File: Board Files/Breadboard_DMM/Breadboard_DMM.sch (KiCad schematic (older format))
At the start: 11 parts

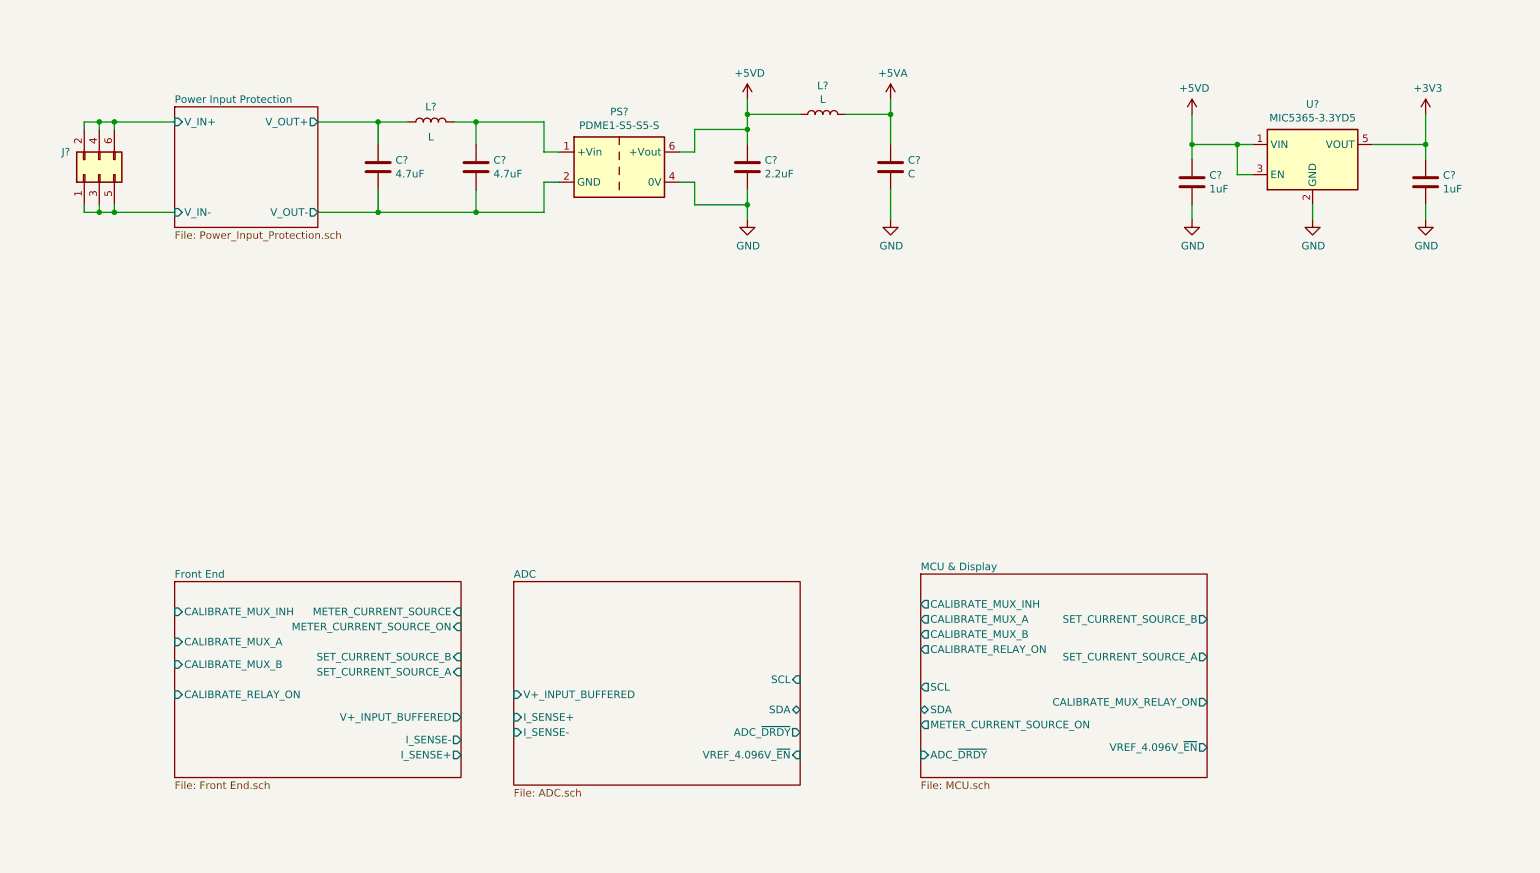
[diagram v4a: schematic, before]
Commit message: Finished main cleanup, started adding digikey part numbers
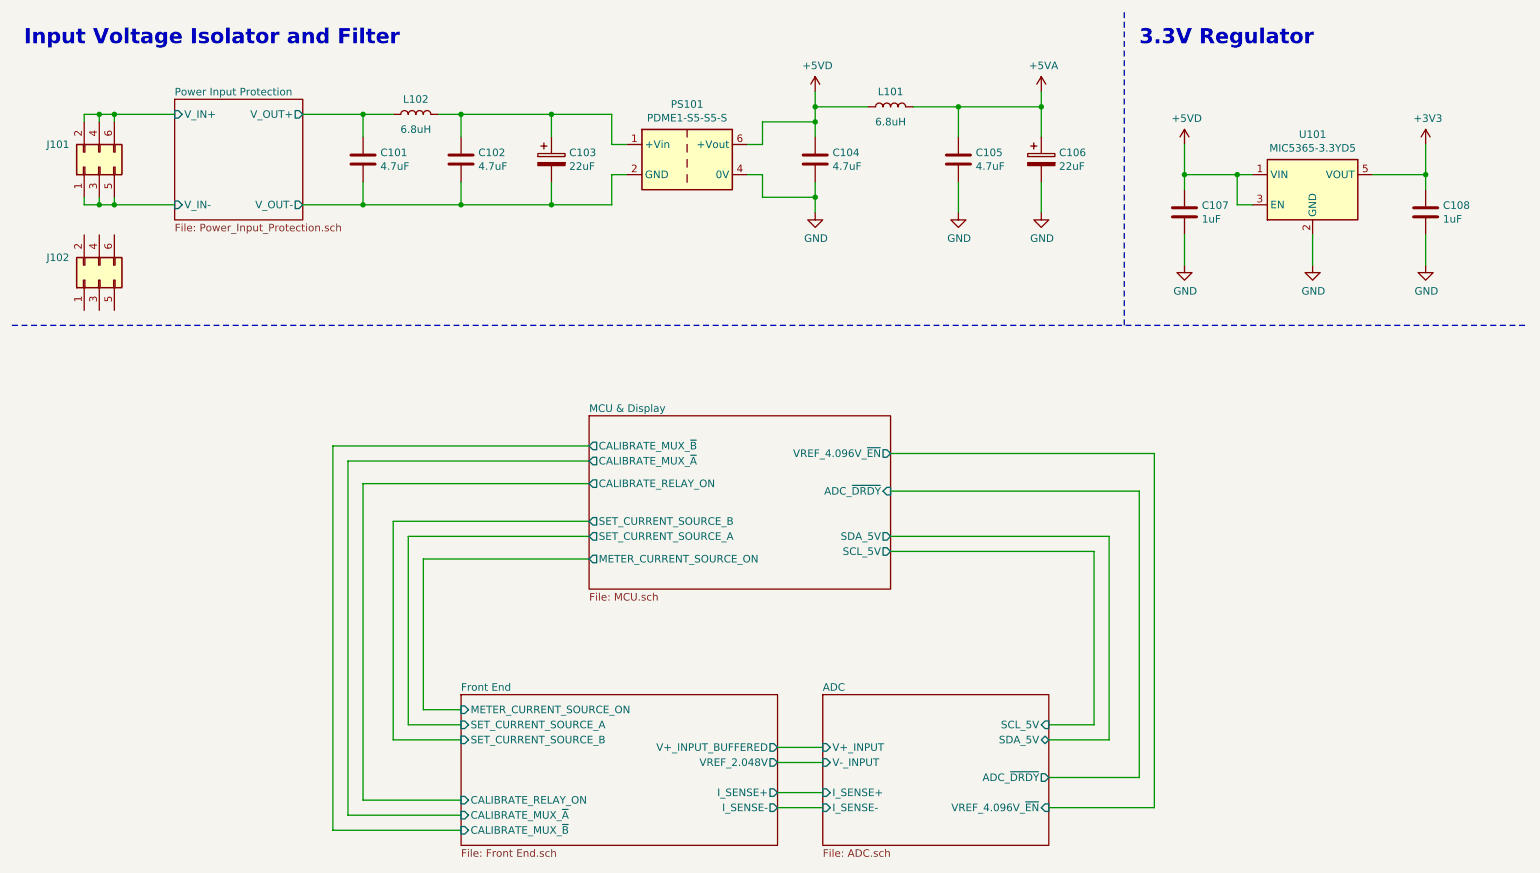
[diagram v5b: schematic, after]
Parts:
- removed C?: 2.2uF, symbol Device:C
- removed C?: C, symbol Device:C
- removed L?: L, symbol Device:L
- added C103, C106: 22uF, Capacitor_SMD:CP_Elec_5x5.3, symbol Device:CP
- added C104, C105: 4.7uF, symbol Device:C
- added J102: Conn_02x03_Odd_Even, symbol Connector_Generic:Conn_02x03_Odd_Even
- added L101: 6.8uH, symbol Device:L
- C101, C102: renamed from C?; Digi-Key Link (none) -> https://www.digikey.com/en/products/detail/samsung-electro-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; Digi-Key PN (none) -> 1276-6462-1-ND
- C107, C108: renamed from C?; Digi-Key PN (none) -> -
- J101: renamed from J?; Digi-Key Link (none) -> https://www.digikey.com/en/products/detail/samtec-inc/TSW-1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; Digi-Key PN (none) -> SAM10846-ND
- L102: renamed from L?; value L -> 6.8uH; Digi-Key PN (none) -> -
- PS101: renamed from PS?; Digi-Key PN (none) -> -
- U101: renamed from U?; Digi-Key PN (none) -> -
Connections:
- net +5VA: now also C105.1, C106.1, L101.2
- net +5VD: now also C104.1, L101.1
- net GND: now also C104.2, C105.2, C106.2
- net Power Input Protection/V_OUT-: now also C103.2
- net at C102.1, L102.2, PS101.1 (+Vin): now also C103.1
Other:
- note added: "3.3V Regulator"
- note added: "Input Voltage Isolator and Filter"
- moved on the sheet: C101, C102, C107, C108, J101, L102, PS101, U101

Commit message: Started adding Digikey links
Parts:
- L101, L102: footprint (none) -> Inductor_SMD:L_0805_2012Metric_Pad1.15x1.40mm_HandSolder; Digi-Key Link (none) -> https://www.digikey.com/en/products/detail/tdk-corporation/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; Digi-Key PN - -> 445-6761-1-ND
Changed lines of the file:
@@
 $Descr USLetter 11000 8500
 encoding utf-8
-Sheet 1 10
+Sheet 1 11
 Title "Toast-O-Meter"
 Date "2020-08-14"
@@
 	1    3450 1450
 	1    0    0    -1
-$EndComp
-$Comp
-L Device:L L102
-U 1 1 5F38DC8E
-P 3150 1150
-F 0 "L102" V 3250 1150 50  0000 C CNN
-F 1 "6.8uH" V 3050 1150 50  0000 C CNN
-F 2 "" H 3150 1150 50  0001 C CNN
-F 3 "~" H 3150 1150 50  0001 C CNN
-F 4 "" H 3150 1150 50  0001 C CNN "Digi-Key Link"
-F 5 "-" H 3150 1150 50  0001 C CNN "Digi-Key PN"
-	1    3150 1150
-	0    -1   -1   0
 $EndComp
 Wire Wire Line
@@
 	1    6750 1450
 	1    0    0    -1
-$EndComp
-$Comp
-L Device:L L101
-U 1 1 600AF036
-P 6300 1100
-F 0 "L101" V 6400 1100 50  0000 C CNN
-F 1 "6.8uH" V 6200 1100 50  0000 C CNN
-F 2 "" H 6300 1100 50  0001 C CNN
-F 3 "~" H 6300 1100 50  0001 C CNN
-F 4 "" H 6300 1100 50  0001 C CNN "Digi-Key Link"
-F 5 "-" H 6300 1100 50  0001 C CNN "Digi-Key PN"
-	1    6300 1100
-	0    -1   -1   0
 $EndComp
 Wire Wire Line
@@
 	1    0    0    -1
 $EndComp
+$Comp
+L Device:L L102
+U 1 1 5F78CC57
+P 3150 1150
+F 0 "L102" V 3250 1150 50  0000 C CNN
+F 1 "6.8uH" V 3050 1150 50  0000 C CNN
+F 2 "Inductor_SMD:L_0805_2012Metric_Pad1.15x1.40mm_HandSolder" H 3150 1150 50  0001 C CNN
+F 3 "~" H 3150 1150 50  0001 C CNN
+F 4 "https://www.digikey.com/en/products/detail/tdk-corporation/MLZ2012N6R8LT000/2523499" H 3150 1150 50  0001 C CNN "Digi-Key Link"
+F 5 "445-6761-1-ND" H 3150 1150 50  0001 C CNN "Digi-Key PN"
+	1    3150 1150
+	0    -1   -1   0
+$EndComp
+$Comp
+L Device:L L101
+U 1 1 5F78D87B
+P 6300 1100
+F 0 "L101" V 6400 1100 50  0000 C CNN
+F 1 "6.8uH" V 6200 1100 50  0000 C CNN
+F 2 "Inductor_SMD:L_0805_2012Metric_Pad1.15x1.40mm_HandSolder" H 6300 1100 50  0001 C CNN
+F 3 "~" H 6300 1100 50  0001 C CNN
+F 4 "https://www.digikey.com/en/products/detail/tdk-corporation/MLZ2012N6R8LT000/2523499" H 6300 1100 50  0001 C CNN "Digi-Key Link"
+F 5 "445-6761-1-ND" H 6300 1100 50  0001 C CNN "Digi-Key PN"
+	1    6300 1100
+	0    -1   -1   0
+$EndComp
 $EndSCHEMATC

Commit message: Finished adding parts, cleaned up, ran ERC
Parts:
- C101, C102, C104, C105: footprint (none) -> Resistor_SMD:R_0805_2012Metric_Pad1.15x1.40mm_HandSolder
- C107, C108: footprint (none) -> Resistor_SMD:R_0603_1608Metric_Pad1.05x0.95mm_HandSolder; Digi-Key Link (none) -> https://www.digikey.com/en/products/detail/samsung-electro-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; Digi-Key PN - -> 1276-6524-1-ND
- J101, J102: footprint (none) -> Connector_PinHeader_2.54mm:PinHeader_2x03_P2.54mm_Vertical; Digi-Key Link https://www.digikey.com/en/products/detail/samtec-inc/TSW-1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 -> https://www.digikey.com/en/products/detail/adam-tech/PH2-06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; Digi-Key PN SAM10846-ND -> 2057-PH2-06-UA-ND
- PS101: Digi-Key Link (none) -> https://www.digikey.com/en/products/detail/cui-inc/PDME1-S5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; Digi-Key PN - -> 102-6320-ND
- U101: Digi-Key Link (none) -> https://www.digikey.com/en/products/detail/microchip-techno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; Digi-Key PN - -> 576-4085-1-ND
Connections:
- net Power Input Protection/V_OUT+ renamed +5VL
- no-connect marks 0 -> 6
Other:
- note added: "Power Supplies / Top Sheet"
- moved on the sheet: C101, C102, C103, C104, C105, C106, C107, C108, J101, J102, L101, L102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

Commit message: Cleaned up files
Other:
- note added: "Sheet 2"
- note added: "Sheet 3"
- note added: "Sheet 7"
- note added: "Sheet 8"
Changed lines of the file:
@@
 Connection ~ 10050 1700
 $Sheet
-S 8300 7150 1500 1000
+S 8300 7150 2250 950
 U 5FDFAE85
 F0 "ADC" 50
@@
 F2 "I_SENSE+" I L 8300 7800 50
 F3 "I_SENSE-" I L 8300 7900 50
-F4 "ADC_~DRDY" O R 9800 7700 50
-F5 "VREF_4.096V_~EN" I R 9800 7900 50
+F4 "ADC_~DRDY" O R 10550 7700 50
+F5 "VREF_4.096V_~EN" I R 10550 7900 50
 F6 "V+_INPUT" I L 8300 7500 50
 F7 "V-_INPUT" I L 8300 7600 50
-F8 "SCL_5V" I R 9800 7350 50
-F9 "SDA_5V" B R 9800 7450 50
+F8 "SCL_5V" I R 10550 7350 50
+F9 "SDA_5V" B R 10550 7450 50
 $EndSheet
 $Comp
@@
 3.3V Regulator
 $Sheet
-S 4850 7150 2100 1000
+S 4850 7150 2600 1000
 U 5F511849
 F0 "Front End" 50
 F1 "Front End.sch" 50
-F2 "V+_INPUT_BUFFERED" O R 6950 7500 50
+F2 "V+_INPUT_BUFFERED" O R 7450 7500 50
 F3 "SET_CURRENT_SOURCE_B" I L 4850 7450 50
 F4 "SET_CURRENT_SOURCE_A" I L 4850 7350 50
@@
 F6 "CALIBRATE_MUX_~A" I L 4850 7950 50
 F7 "CALIBRATE_MUX_~B" I L 4850 8050 50
-F8 "I_SENSE+" O R 6950 7800 50
-F9 "I_SENSE-" O R 6950 7900 50
+F8 "I_SENSE+" O R 7450 7800 50
+F9 "I_SENSE-" O R 7450 7900 50
 F10 "METER_CURRENT_SOURCE_ON" I L 4850 7250 50
-F11 "VREF_2.048V" O R 6950 7600 50
+F11 "VREF_2.048V" O R 7450 7600 50
 $EndSheet
-Wire Wire Line
-	8300 7900 6950 7900
-Wire Wire Line
-	6950 7600 8300 7600
-Wire Wire Line
-	6950 7500 8300 7500
-Wire Wire Line
-	6950 7800 8300 7800
 $Sheet
-S 6500 5300 2000 1150
+S 6250 5300 2700 1150
 U 5F3FD151
 F0 "MCU & Display" 50
 F1 "MCU.sch" 50
-F2 "CALIBRATE_RELAY_ON" O L 6500 5750 50
-F3 "METER_CURRENT_SOURCE_ON" O L 6500 6250 50
-F4 "ADC_~DRDY" I R 8500 5800 50
-F5 "SET_CURRENT_SOURCE_B" O L 6500 6000 50
-F6 "SET_CURRENT_SOURCE_A" O L 6500 6100 50
-F7 "VREF_4.096V_~EN" O R 8500 5550 50
-F8 "SCL_5V" O R 8500 6200 50
-F9 "SDA_5V" O R 8500 6100 50
-F10 "CALIBRATE_MUX_~B" O L 6500 5500 50
-F11 "CALIBRATE_MUX_~A" O L 6500 5600 50
+F2 "CALIBRATE_RELAY_ON" O L 6250 5750 50
+F3 "METER_CURRENT_SOURCE_ON" O L 6250 6250 50
+F4 "ADC_~DRDY" I R 8950 5800 50
+F5 "SET_CURRENT_SOURCE_B" O L 6250 6000 50
+F6 "SET_CURRENT_SOURCE_A" O L 6250 6100 50
+F7 "VREF_4.096V_~EN" O R 8950 5550 50
+F8 "SCL_5V" O R 8950 6200 50
+F9 "SDA_5V" O R 8950 6100 50
+F10 "CALIBRATE_MUX_~B" O L 6250 5500 50
+F11 "CALIBRATE_MUX_~A" O L 6250 5600 50
 $EndSheet
 Wire Wire Line
-	10500 5550 8500 5550
-Wire Wire Line
-	10500 7900 10500 5550
-Wire Wire Line
-	9800 7900 10500 7900
-Wire Wire Line
-	10400 7700 9800 7700
-Wire Wire Line
-	10400 5800 10400 7700
-Wire Wire Line
-	8500 5800 10400 5800
-Wire Wire Line
-	10200 7450 9800 7450
-Wire Wire Line
-	10200 6100 10200 7450
-Wire Wire Line
-	8500 6100 10200 6100
-Wire Wire Line
-	10100 7350 9800 7350
-Wire Wire Line
-	10100 6200 10100 7350
-Wire Wire Line
-	8500 6200 10100 6200
-Wire Wire Line
-	4000 5500 6500 5500
+	11250 7900 11250 5550
+Wire Wire Line
+	11150 5800 11150 7700
+Wire Wire Line
+	10950 6100 10950 7450
+Wire Wire Line
+	10850 6200 10850 7350
+Wire Wire Line
+	4000 5500 6250 5500
 Wire Wire Line
 	4000 8050 4000 5500
@@
 	4100 5600 4100 7950
 Wire Wire Line
-	6500 5600 4100 5600
+	6250 5600 4100 5600
 Wire Wire Line
 	4200 7850 4850 7850
@@
 	4200 5750 4200 7850
 Wire Wire Line
-	6500 5750 4200 5750
+	6250 5750 4200 5750
 Wire Wire Line
 	4400 7450 4850 7450
@@
 	4400 6000 4400 7450
 Wire Wire Line
-	6500 6000 4400 6000
+	6250 6000 4400 6000
 Wire Wire Line
 	4500 7350 4850 7350
@@
 	4500 6100 4500 7350
 Wire Wire Line
-	6500 6100 4500 6100
+	6250 6100 4500 6100
 Wire Wire Line
 	4600 7250 4850 7250
@@
 	4600 6250 4600 7250
 Wire Wire Line
-	6500 6250 4600 6250
+	6250 6250 4600 6250
 $Comp
 L Connector_Generic:Conn_02x03_Odd_Even J102
@@
 Wire Wire Line
 	9800 1700 10050 1700
+Wire Wire Line
+	10850 6200 8950 6200
+Wire Wire Line
+	8950 6100 10950 6100
+Wire Wire Line
+	11150 5800 8950 5800
+Wire Wire Line
+	8950 5550 11250 5550
+Wire Wire Line
+	10550 7350 10850 7350
+Wire Wire Line
+	10950 7450 10550 7450
+Wire Wire Line
+	10550 7700 11150 7700
+Wire Wire Line
+	11250 7900 10550 7900
+Wire Wire Line
+	7450 7500 8300 7500
+Wire Wire Line
+	8300 7600 7450 7600
+Wire Wire Line
+	7450 7800 8300 7800
+Wire Wire Line
+	7450 7900 8300 7900
+Text Notes 8350 5250 0    100  ~ 20
+Sheet 7
+Text Notes 9950 7100 0    100  ~ 20
+Sheet 2
+Text Notes 2500 1650 0    100  ~ 20
+Sheet 8
+Text Notes 6850 7100 0    100  ~ 20
+Sheet 3
 $EndSCHEMATC
